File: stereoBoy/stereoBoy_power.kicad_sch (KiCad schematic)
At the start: 40 parts, among them J1 Conn_01x02, J4 Conn_01x04, J7 USB_C_Receptacle_USB2.0_16P, J9 Conn_01x06, Q2 MMUN2133LT1, U10 MCP73871, U11 TPS61091, U15 AP2112K-3.3

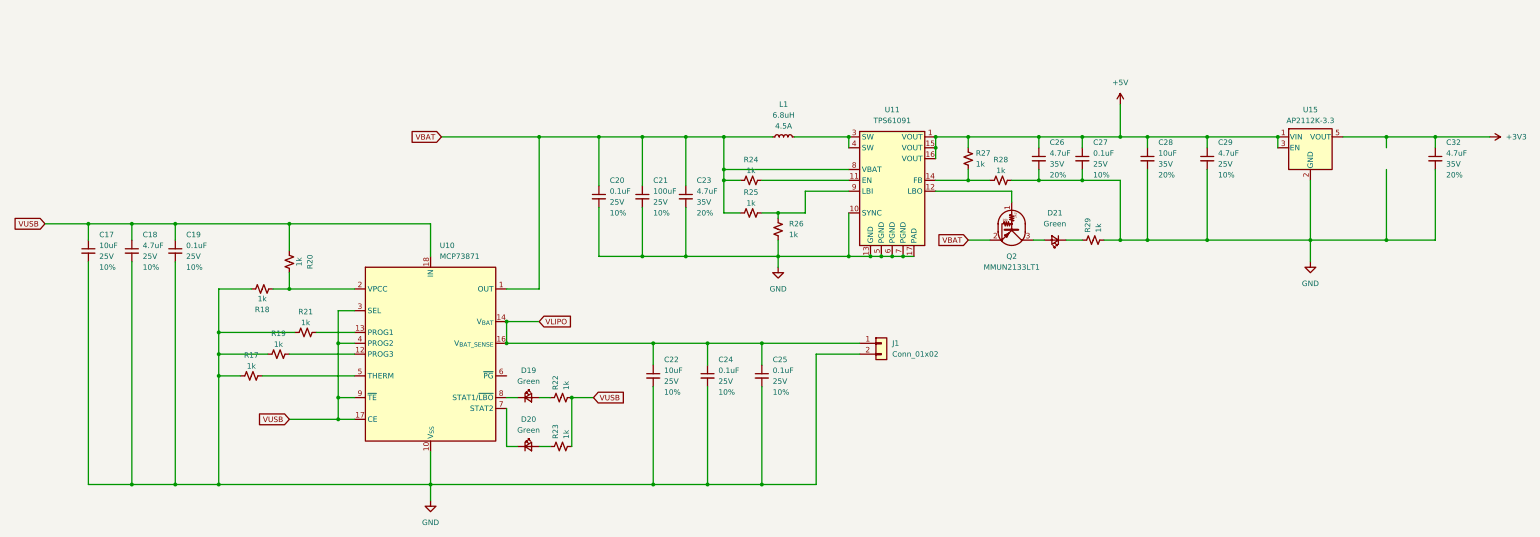
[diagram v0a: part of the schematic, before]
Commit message: redesigned PSU for AAAs
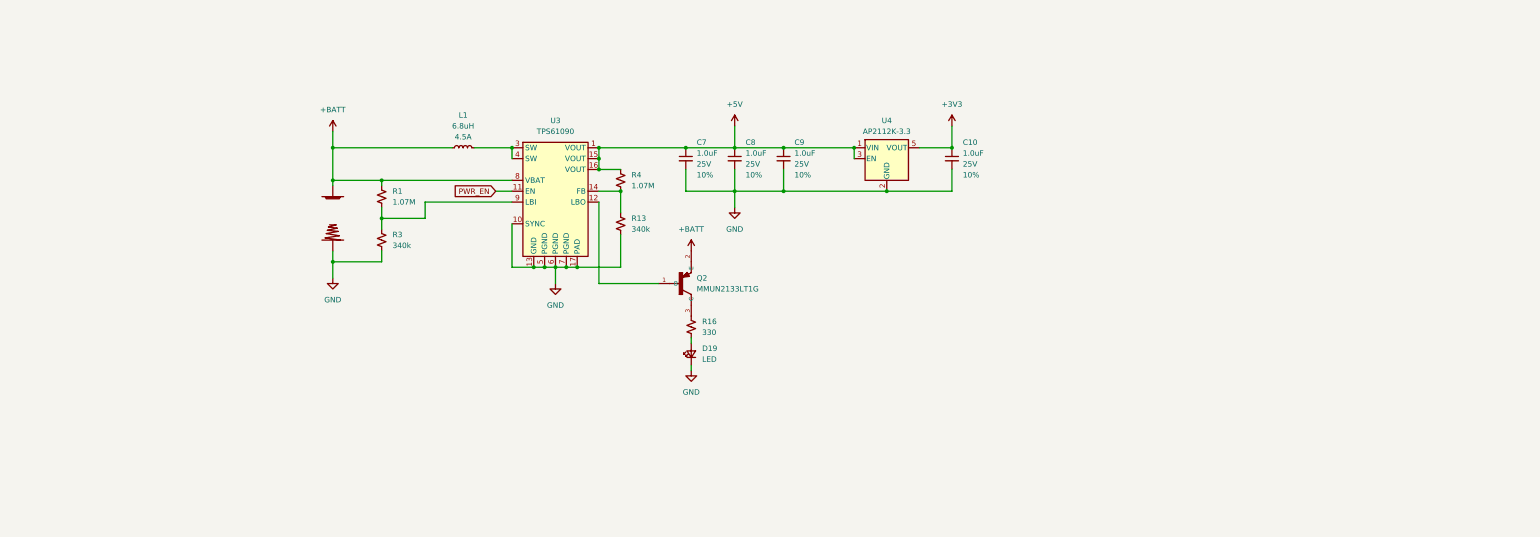
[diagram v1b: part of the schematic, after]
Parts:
- removed C17: 10uF, SparkFun-Capacitor:C_0805_2012Metric, symbol SparkFun-Capacitor:1.0uF_0805_25V_10%
- removed C18, C29: 4.7uF, SparkFun-Capacitor:C_0805_2012Metric, symbol SparkFun-Capacitor:1.0uF_0805_25V_10%
- removed C19, C20, C24, C27: 0.1uF, SparkFun-Capacitor:C_0805_2012Metric, symbol SparkFun-Capacitor:1.0uF_0805_25V_10%
- removed C21: 100uF, SparkFun-Capacitor:C_0805_2012Metric, symbol SparkFun-Capacitor:1.0uF_0805_25V_10%
- removed C22: 10uF, Capacitor_SMD:C_0603_1608Metric, symbol SparkFun-Capacitor:1.0uF_0805_25V_10%
- removed C23, C26: 4.7uF, SparkFun-Capacitor:C_0603_1608Metric, symbol SparkFun-Capacitor:4.7uF_0603_35V_20%
- removed C25: 0.1uF, Capacitor_SMD:C_0805_2012Metric, symbol SparkFun-Capacitor:1.0uF_0805_25V_10%
- removed C28: 10uF, SparkFun-Capacitor:C_0603_1608Metric, symbol SparkFun-Capacitor:4.7uF_0603_35V_20%
- removed C32: 4.7uF, Capacitor_SMD:C_0805_2012Metric, symbol SparkFun-Capacitor:4.7uF_0603_35V_20%
- removed D19, D20, D21: Green, SparkFun-LED:LED_0603_1608Metric_Green, symbol SparkFun-LED:LED_Green_0603
- removed J1: Conn_01x02, Connector_JST:JST_PH_S2B-PH-K_1x02_P2.00mm_Horizontal, symbol SparkFun-Connector:Conn_01x02
- removed Q2: MMUN2133LT1, Package_TO_SOT_SMD:SOT-23, symbol Transistor_BJT:DTB123Y
- removed R17, R18, R19, R20, R21, R22, R23, R24, R25, R26, R27, R28, R29: 1k, SparkFun-Resistor:R_0603_1608Metric, symbol SparkFun-Resistor:1k_0603
- removed U10: MCP73871, Package_DFN_QFN:QFN-20-1EP_4x4mm_P0.5mm_EP2.5x2.5mm, symbol Battery_Management:MCP73871
- removed U11: TPS61091, Package_DFN_QFN:Texas_RSA_VQFN-16-1EP_4x4mm_P0.65mm_EP2.7x2.7mm_ThermalVias, symbol Regulator_Switching:TPS61091
- removed U15: AP2112K-3.3, Package_TO_SOT_SMD:SOT-23-5, symbol Regulator_Linear:AP2112K-3.3
- added +0: MGB+BATTERY4, MGBC-MBL-01_2_1:MGB+BATTERY4, symbol MGBC-MBL-01_2_1-eagle-import:MGB+BATTERY4
- added -0: MGB-BATTERY4, MGBC-MBL-01_2_1:MGB-BATTERY4, symbol MGBC-MBL-01_2_1-eagle-import:MGB-BATTERY4
- added C10, C7, C8, C9: 1.0uF, SparkFun-Capacitor:C_0805_2012Metric, symbol SparkFun-Capacitor:1.0uF_0805_25V_10%
- added D19: LED, SparkFun-LED:LED_0603_1608Metric, symbol SparkFun-LED:LED
- added Q2: MMUN2133LT1G, MMUN2133LT1G:SOT95P240X111-3N, symbol MMUN2133LT1G:MMUN2133LT1G
- added R1, R4: 1.07M, SparkFun-Resistor:R_0603_1608Metric, symbol SparkFun-Resistor:1k_0603
- added R13, R3: 340k, SparkFun-Resistor:R_0603_1608Metric, symbol SparkFun-Resistor:1k_0603
- added R16: 330, SparkFun-Resistor:R_0603_1608Metric, symbol SparkFun-Resistor:1k_0603
- added U3: TPS61090, Package_DFN_QFN:Texas_RSA_VQFN-16-1EP_4x4mm_P0.65mm_EP2.7x2.7mm_ThermalVias, symbol Regulator_Switching:TPS61090
- added U4: AP2112K-3.3, Package_TO_SOT_SMD:SOT-23-5, symbol Regulator_Linear:AP2112K-3.3
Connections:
- net +3V3: now also C10.1, U4.5 (VOUT)
- net +5V: now also C7.1, C8.1, C9.1, R4.1, U3.1 (VOUT), U3.15 (VOUT), U3.16 (VOUT), U4.1 (VIN), U4.3 (EN)
- net GND: now also -0.P$1, -0.P$3 (P$1), -0.P$4 (P$1), C10.2, C7.2, C8.2, C9.2, D19.1 (K), R13.2, R3.2, U3.10 (SYNC), U3.13 (GND), U3.17 (PAD), U3.5 (PGND), U3.6 (PGND), U3.7 (PGND), U4.2 (GND)
- net at L1.2: now also U3.3 (SW), U3.4 (SW)
- net VBAT renamed +BATT
- net +BATT: now also +0.P$1, +0.P$2 (P$1), +0.P$3 (P$1), Q2.2 (E), R1.1, U3.8 (VBAT)
- new net: Q2.3 (C), R16.1
- new net: D19.2 (A), R16.2
- new net: R13.1, R4.2, U3.14 (FB)
- new net: R1.2, R3.1, U3.9 (LBI)
- new net: Q2.1 (B), U3.12 (LBO)
- new net PWR_EN: U3.11 (EN)

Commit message: yeah
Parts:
- removed J4: Conn_01x04, Connector_PinHeader_2.54mm:PinHeader_1x04_P2.54mm_Vertical, symbol SparkFun-Connector:Conn_01x04
- removed J9: Conn_01x06, SparkFun-Connector:1x06, symbol SparkFun-Connector:Conn_01x06
- added C1, C2: 47uF, Capacitor_Tantalum_SMD:CP_EIA-7343-15_Kemet-W_HandSolder, symbol SparkFun-Capacitor:47uF_3528_10V_10%
- added C11, C12, C13: 1.0uF, SparkFun-Capacitor:C_0805_2012Metric, symbol SparkFun-Capacitor:1.0uF_0805_25V_10%
- added L2, L3: 600 Ohm, SparkFun-Capacitor:C_0805_2012Metric, symbol SparkFun-Coil:Ferrite_600Ohm_0805_500mA
- added U8: AP2112K-1.8, Package_TO_SOT_SMD:SOT-23-5, symbol Regulator_Linear:AP2112K-1.8
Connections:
- net +3V3: now also L2.1
- net +5V: now also C11.1, U8.1 (VIN), U8.3 (EN)
- net +BATT: now also C1.1, C2.1
- net GND: now also C1.2, C11.2, C12.2, C2.2, L3.1, U8.2 (GND)
- new net +1V8: C12.1, U8.5 (VOUT)
- new net GNDA: C13.2, L3.2
- new net VDDA: C13.1, L2.2
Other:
- moved on the sheet: C10, C9, J7, U4, ZOOM_CAP1

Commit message: yuh
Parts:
- removed C13: 1.0uF, SparkFun-Capacitor:C_0805_2012Metric, symbol SparkFun-Capacitor:1.0uF_0805_25V_10%
- removed D19: LED, SparkFun-LED:LED_0603_1608Metric, symbol SparkFun-LED:LED
- removed Q2: MMUN2133LT1G, MMUN2133LT1G:SOT95P240X111-3N, symbol MMUN2133LT1G:MMUN2133LT1G
- removed U4: AP2112K-3.3, Package_TO_SOT_SMD:SOT-23-5, symbol Regulator_Linear:AP2112K-3.3
- removed U8: AP2112K-1.8, Package_TO_SOT_SMD:SOT-23-5, symbol Regulator_Linear:AP2112K-1.8
- added C28: 0.1uF, Capacitor_Tantalum_SMD:CP_EIA-6032-20_AVX-F, symbol SparkFun-Capacitor:47uF_3528_10V_10%
- added C30: 10uF, Capacitor_Tantalum_SMD:CP_EIA-6032-20_AVX-F, symbol SparkFun-Capacitor:47uF_3528_10V_10%
- added C42: 1.0uF, SparkFun-Capacitor:C_0805_2012Metric, symbol SparkFun-Capacitor:1.0uF_0805_25V_10%
- added C48: 4.7uF, SparkFun-Capacitor:C_0805_2012Metric, symbol SparkFun-Capacitor:1.0uF_0805_25V_10%
- added C68, C76: 1.0uF, Capacitor_SMD:C_0805_2012Metric, symbol SparkFun-Capacitor:1.0uF_0805_25V_10%
- added C77, C78, C80: 0.1uF, SparkFun-Capacitor:C_1206_3216Metric, symbol SparkFun-Capacitor:1.0uF_0805_25V_10%
- added D19, D20, D21: Green, SparkFun-LED:LED_0603_1608Metric_Green, symbol SparkFun-LED:LED_Green_0603
- added H1, H2: MountingHole_Pad_MP, MountingHole:MountingHole_2.7mm_M2.5_Pad_TopBottom, symbol Mechanical:MountingHole_Pad_MP
- added L4, L5: 2.2uH, Inductor_SMD:L_APV_ANR4020, symbol SparkFun-Coil:10uH_0805_0.35A
- added L6: 600Ω @ 100MHz, Capacitor_SMD:C_0603_1608Metric, symbol SparkFun-Coil:Ferrite_600Ohm_0805_500mA
- added L7: 600Ω @ 100MHz, Inductor_SMD:L_0603_1608Metric, symbol SparkFun-Coil:Ferrite_600Ohm_0805_500mA
- added Q2: FDN306P, Package_TO_SOT_SMD:SOT-23, symbol Transistor_FET:FDN340P
- added R14, R15: 22, Capacitor_SMD:C_0402_1005Metric, symbol SparkFun-Resistor:27_0603
- added R33: 5.1k, SparkFun-Resistor:R_0603_1608Metric, symbol SparkFun-Resistor:1k_0603
- added R35: 453k, SparkFun-Resistor:R_0603_1608Metric, symbol SparkFun-Resistor:1k_0603
- added R36, R38: 100k, SparkFun-Resistor:R_0603_1608Metric, symbol SparkFun-Resistor:1k_0603
- added R37: 200k, SparkFun-Resistor:R_0603_1608Metric, symbol SparkFun-Resistor:1k_0603
- added R41, R42, R43: 330, SparkFun-Resistor:R_0402_1005Metric, symbol SparkFun-Resistor:33_0603
- added R44: 100k, SparkFun-Resistor:R_0805_2012Metric, symbol SparkFun-Resistor:1k_0603
- added R54, R55, R56: 1.4M, SparkFun-Resistor:R_0402_1005Metric, symbol SparkFun-Resistor:1k_0603
- added SW3: MGB-SW1, MIN_WORKS:GBP_Power_Switch, symbol MGBC-MBL-01_2_1-eagle-import:MGB-SW1
- added TP13, TP16, TP17, TP3, TP30, TP4, TP5, TP6, TP7, TP8, TP9: TestPoint_Alt, TestPoint:TestPoint_Pad_1.5x1.5mm, symbol Connector:TestPoint_Alt
- added TP26: TestPoint_Alt, TestPoint:TestPoint_Pad_D1.0mm, symbol Connector:TestPoint_Alt
- added U12: USBLC6-2P6, Package_TO_SOT_SMD:SOT-666, symbol Power_Protection:USBLC6-2P6
- added U4, U8: TLV62569DBV, Package_TO_SOT_SMD:SOT-23-5, symbol Regulator_Switching:TLV62569DBV
- added U7: TPS2116DRL, Package_TO_SOT_SMD:SOT-583-8, symbol Power_Management:TPS2116DRL
- C1: value 47uF -> 100uF
- C10, C12: value 1.0uF -> 6.8pF
- C11, C9: value 1.0uF -> 4.7uF
- C7: value 1.0uF -> 0.1uF; footprint SparkFun-Capacitor:C_0805_2012Metric -> SparkFun-Capacitor:C_1206_3216Metric
- C8: value 1.0uF -> 0.1uF
- L2: value 600 Ohm -> 600Ω @ 100MHz; footprint SparkFun-Capacitor:C_0805_2012Metric -> Capacitor_SMD:C_0603_1608Metric; Frequency 100MHz -> (none)
- L3: value 600 Ohm -> 600Ω @ 100MHz; footprint SparkFun-Capacitor:C_0805_2012Metric -> Inductor_SMD:L_0603_1608Metric; Frequency 100MHz -> (none)
- R1: value 1.07M -> 1.4M
- R13: value 340k -> 180k
- R16: value 330 -> 5.1k
- R3: value 340k -> 390k
- R4: value 1.07M -> 1.62M
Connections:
- net VDDA is gone; now on net +3V3: L2.2
- net +1V8: now also L6.2, R43.2, TP26.1, TP9.1; no longer C12.1
- net +3V3: now also R42.2, SW3.P$1 (1), TP13.1; no longer C10.1, L2.1
- net +5V: now also C2.1, L7.1, TP16.1; no longer C11.1, C7.1, C8.1, C9.1, R4.1, U3.1 (VOUT), U3.15 (VOUT), U3.16 (VOUT)
- net +BATT: now also C1.2, C28.2, C30.2, Q2.2 (S), R54.2, TP7.1; no longer +0.P$1, +0.P$2 (P$1), +0.P$3 (P$1), C1.1, C2.1
- net GND: now also C1.1, R16.2, C28.1, C30.1, C42.2, C48.2, C68.2, C76.2, C77.2, C78.2, C80.2, D19.1 (K), D20.1 (K), D21.1 (K), H1.MP, H2.MP, R33.2, R36.2, R38.2, R44.1, R56.2, SW3.P$3 (3), TP30.1, U12.2 (GND), U4.2 (GND), U7.1 (GND), U8.2 (GND); no longer C1.2, C10.2, C12.2, L3.1
- net PWR_EN: now also R54.1, SW3.P$C (C), TP3.1
- net USB_DM: now also U12.6 (I/O1)
- net USB_DP: now also U12.4 (I/O2)
- net at R16.1: now also J7.A5 (CC1)
- net LOW_BATT: now reaches U3.12 (LBO)
- net LOW_BATT: now also TP4.1
- net at J7.B5 (CC2): now also R33.1
- net GNDA renamed +5V_OUT
- net +5V_OUT: now also C11.1, C9.1, C42.1, C77.1, C78.1, C80.1, L7.2, U4.1 (EN), U4.4 (VIN), U7.2 (VOUT), U7.7 (VOUT), U8.1 (EN), U8.4 (VIN)
- net VUSB renamed VBUS
- net VBUS: now also C68.1, C76.1, R55.1, TP6.1, U12.5 (VBUS), U7.3 (VIN1), U7.5 (MODE)
- new net: Q2.1 (G), R44.2
- new net: R14.2, U12.1 (I/O1)
- new net: R15.2, U12.3 (I/O2)
- new net: C10.1, L2.1, L4.2, R35.1
- new net: C10.2, R35.2, R36.1, U4.5 (FB)
- new net: D19.2 (A), R41.1
- new net: L4.1, U4.3 (SW)
- new net: D20.2 (A), R42.1
- new net: R55.2, R56.1, U7.4 (PR1)
- new net: +0.P$1, +0.P$2 (P$1), +0.P$3 (P$1), Q2.3 (D)
- new net: C12.1, L5.2, L6.1, R37.1
- new net: C12.2, R37.2, R38.1, U8.5 (FB)
- new net: D21.2 (A), R43.1
- new net: L5.1, U8.3 (SW)
- new net +5V_BUCK: C48.1, C7.1, C8.1, R4.1, TP5.1, U3.1 (VOUT), U3.15 (VOUT), U3.16 (VOUT), U7.6 (VIN2)
- new net +5V_SPK: L3.1, R41.2, TP8.1
- new net USB_DM_STM32: R14.1
- new net USB_DP_STM32: R15.1
- new net VIN1_ON: TP17.1, U7.8 (ST)
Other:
- note added: "+"
- note added: "-"
- note added: "2.2uH, 5.5A 4mm x 4mm inductor"
- note added: "BOOST CONVERTER"
- note added: "Boosts 2xAAA (3V) to 5V"
- note added: "Chooses USB over battery"
- note added: "Converts 5V to 3.3V and 1.8V"
- note added: "LDO"
- note added: "Low Batt threshold: 2.3V"
- note added: "OR CONTRLLER"
- note added: "P-Channel MOSFET: Vsd conducts when Gate (Pin 1) is lower than Source (Pin 3) Used here as basic reverse polarity protection"
- note added: "POWER SWITCH"
- note added: "PR1 = 1, so VIN1 priority"
- note added: "Reverse polarity verified with simulation"
- note added: "STATUS LEDS"
- note added: "STEREOBOY"
- note added: "STEREOBOY POWER SUPPLY"
- note added: "TEST PADS"
- note added: "TPS61090 Notes -> 500mA+ from 1.8V -> 95% eff at 5V 200mA out"
- note added: "USB Type-C"
- note added: "Verified!"
- note added: "Vout: 5.1V"
- note added: "with Adafruit Powerboost 500 basic"
- note added: "with Adafruit TLV62565 modified for 3.3V and 1.8V"
- moved on the sheet: C1, C10, C2, C7, C8, C9, J7, L1, L2, R1, R13, R3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

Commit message: yuh
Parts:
- removed H1, H2: MountingHole_Pad_MP, MountingHole:MountingHole_2.7mm_M2.5_Pad_TopBottom, symbol Mechanical:MountingHole_Pad_MP
- removed TP6: TestPoint_Alt, TestPoint:TestPoint_Pad_1.5x1.5mm, symbol Connector:TestPoint_Alt
- removed ZOOM_CAP1: 4.7uF, Capacitor_SMD:C_0805_2012Metric, symbol SparkFun-Capacitor:1.0uF_0805_25V_10%
- added C63: 2.2uF, SparkFun-Capacitor:C_0603_1608Metric, symbol SparkFun-Capacitor:1.0uF_0805_25V_10%
- added D22: BAT60JFILM, SparkFun-Semiconductor-Standard:SOD-323, symbol SparkFun-DiscreteSemi:D_Schottky_3A_10V_0.28V
- C48: value 4.7uF -> 100uF
- C7: footprint SparkFun-Capacitor:C_1206_3216Metric -> SparkFun-Capacitor:C_0603_1608Metric
- C8: value 0.1uF -> 47uF
- R54: value 1.4M -> 10K
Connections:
- net +3V3: no longer SW3.P$1 (1)
- net +5V_BUCK: now also C63.1
- net +BATT: now also SW3.P$1 (1)
- net GND: now also C63.2
- net USB_DM: now also U12.4 (I/O2); no longer U12.6 (I/O1)
- net USB_DM_STM32: now also R15.1; no longer R14.1
- net USB_DP: now also U12.6 (I/O1); no longer U12.4 (I/O2)
- net USB_DP_STM32: now also R14.1; no longer R15.1
- net VBUS: now also D22.1 (K); no longer C68.1, C76.1, J7.A4 (VBUS), J7.A9 (VBUS), J7.B4 (VBUS), J7.B9 (VBUS), U12.5 (VBUS)
- new net VBUS_RAW: C68.1, C76.1, D22.2 (A), J7.A4 (VBUS), J7.A9 (VBUS), J7.B4 (VBUS), J7.B9 (VBUS), U12.5 (VBUS)
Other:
- moved on the sheet: R13, R14, R15, R4, U12
